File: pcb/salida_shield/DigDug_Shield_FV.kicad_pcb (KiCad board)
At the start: 2 copper layers, 68.6 x 53.3 mm, 15 parts, among them J1 Header hembra 1x04 2.54mm, J2 Header hembra 1x04 2.54mm, J3 Bornera 3 polos 5.08mm, J4 Bornera 2 polos 5.08mm, J5 Header apilable 1x10, J6 Header apilable 1x08, J7 Header apilable 1x08, J8 Header apilable 1x06

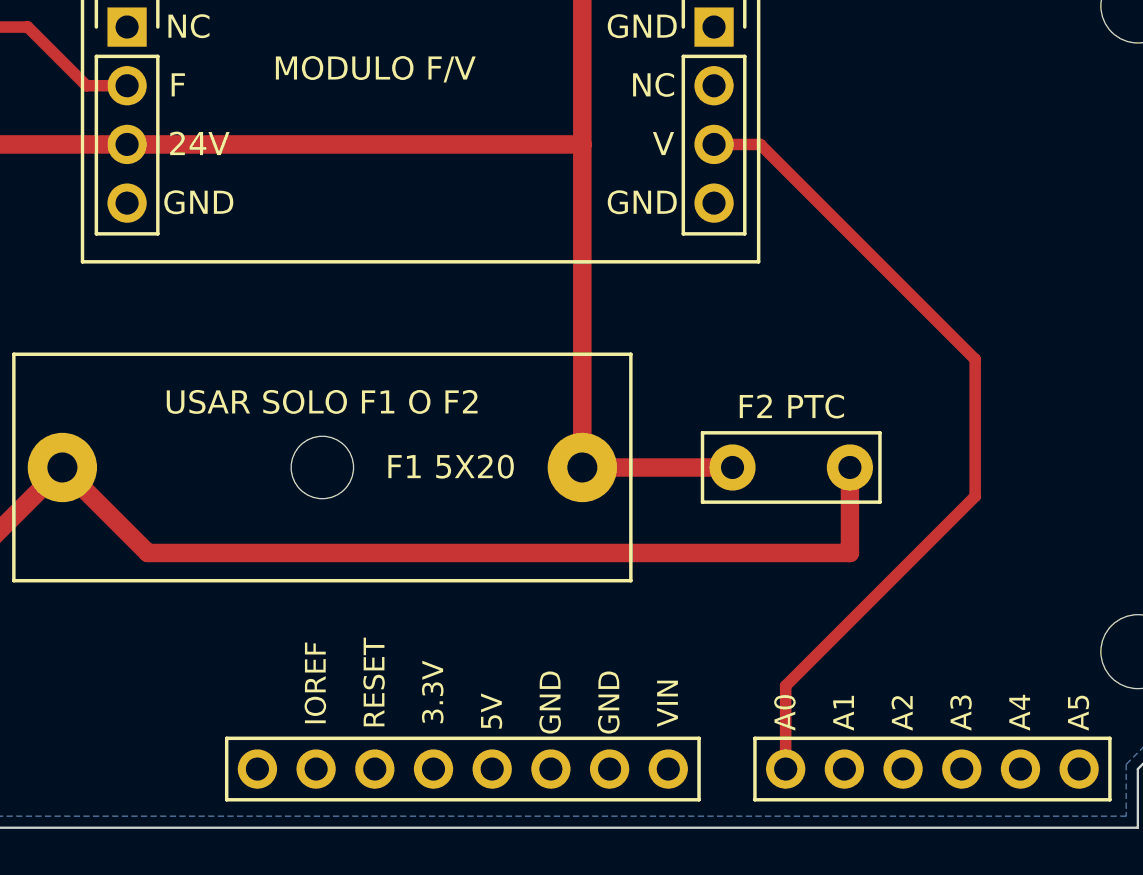
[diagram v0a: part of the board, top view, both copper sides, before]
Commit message: Shield F/V: alejar la pista de A0 de la de 24V
La pista V -> A0 rodea a F2 más a la derecha (x = 60 mm) y la esquina de la
pista de 24V de entrada que va a F2 quedó recortada a 45°. La separación
entre A0 y 24V pasa de 1.45 mm a 3.29 mm.

Co-Authored-By: Claude Opus 5.5 <noreply@anthropic.com>
Claude-Session: https://claude.ai/code/session_013rdDFcXVNHwPZ276iVaQeY
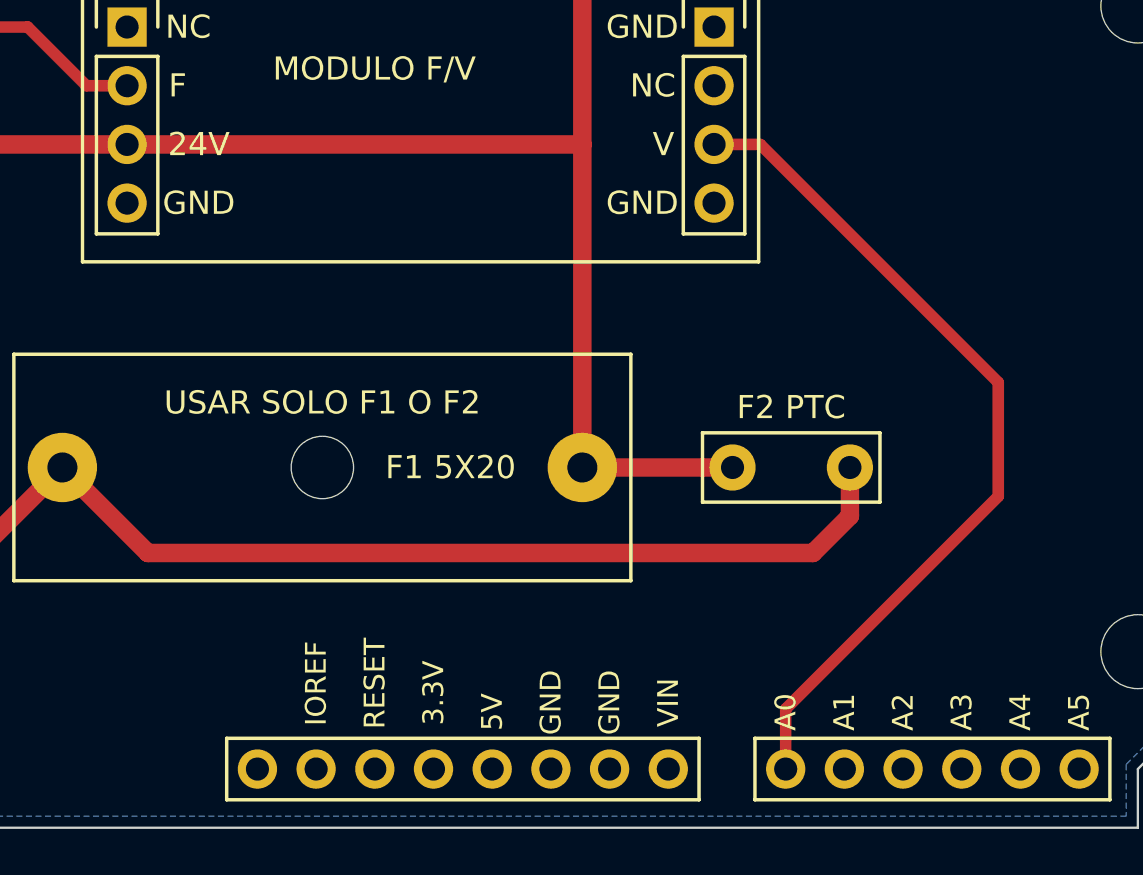
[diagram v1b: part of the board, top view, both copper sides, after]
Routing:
- net +24V_IN: track 55.0 -> 54.1 mm
- net A0: track 36.3 -> 37.1 mm
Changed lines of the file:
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@@
   (segment (start 142 123.77) (end 122.3 123.77) (width 0.8) (layer "F.Cu") (net 4))
   (segment (start 119.5 137.75) (end 123.2 141.45) (width 0.8) (layer "F.Cu") (net 5))
-  (segment (start 123.2 141.45) (end 153.58 141.45) (width 0.8) (layer "F.Cu") (net 5))
-  (segment (start 153.58 141.45) (end 153.58 137.75) (width 0.8) (layer "F.Cu") (net 5))
+  (segment (start 123.2 141.45) (end 151.98 141.45) (width 0.8) (layer "F.Cu") (net 5))
+  (segment (start 151.98 141.45) (end 153.58 139.85) (width 0.8) (layer "F.Cu") (net 5))
+  (segment (start 153.58 139.85) (end 153.58 137.75) (width 0.8) (layer "F.Cu") (net 5))
   (segment (start 148.5 137.75) (end 142 137.75) (width 0.8) (layer "F.Cu") (net 4))
   (segment (start 142 123.77) (end 142 113) (width 0.8) (layer "F.Cu") (net 4))
@@
   (segment (start 105.5 123.77) (end 122.3 123.77) (width 0.8) (layer "F.Cu") (net 4))
   (segment (start 147.7 123.77) (end 149.7 123.77) (width 0.5) (layer "F.Cu") (net 2))
-  (segment (start 149.7 123.77) (end 159 133.07) (width 0.5) (layer "F.Cu") (net 2))
-  (segment (start 159 133.07) (end 159 139) (width 0.5) (layer "F.Cu") (net 2))
-  (segment (start 159 139) (end 150.8 147.2) (width 0.5) (layer "F.Cu") (net 2))
-  (segment (start 150.8 147.2) (end 150.8 150.8) (width 0.5) (layer "F.Cu") (net 2))
+  (segment (start 149.7 123.77) (end 160 134.07) (width 0.5) (layer "F.Cu") (net 2))
+  (segment (start 160 134.07) (end 160 139) (width 0.5) (layer "F.Cu") (net 2))
+  (segment (start 160 139) (end 150.8 148.2) (width 0.5) (layer "F.Cu") (net 2))
+  (segment (start 150.8 148.2) (end 150.8 150.8) (width 0.5) (layer "F.Cu") (net 2))
 )
